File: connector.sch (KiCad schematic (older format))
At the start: 3 parts, among them J1 DB26_Male_HighDensity_Mountin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, J6 Conn_02x02_Odd_Even, SW3 SW_DIP_x03

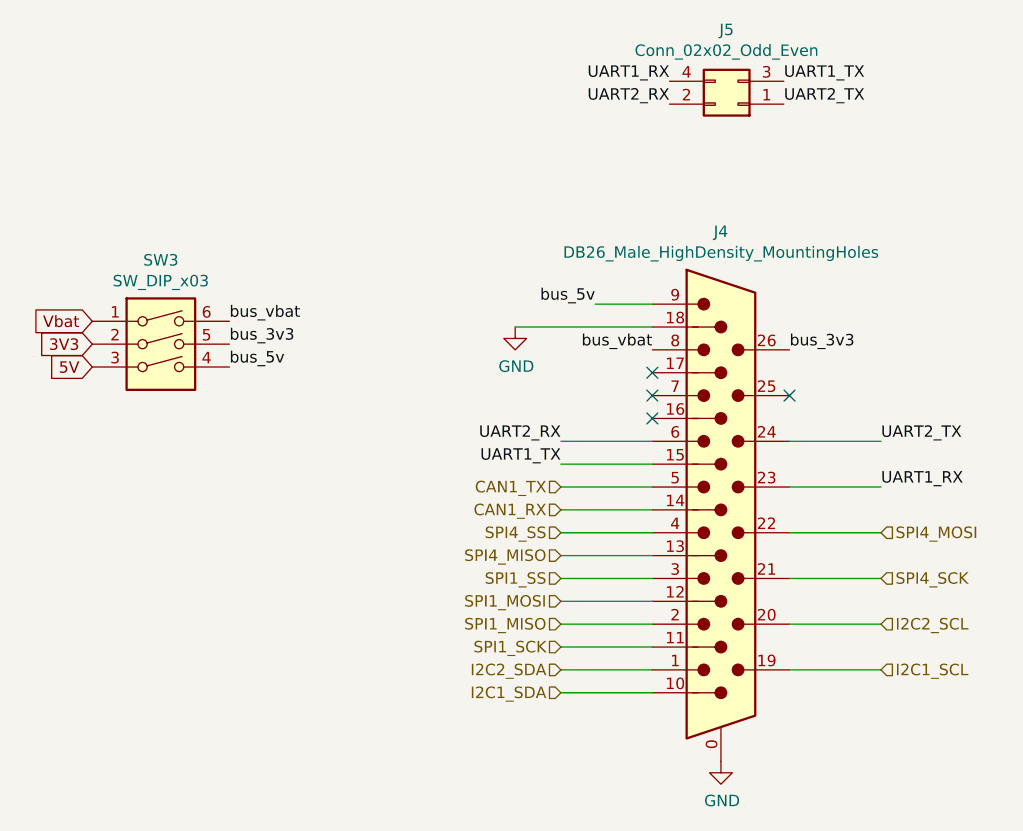
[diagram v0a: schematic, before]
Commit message: Change DB-26-HD footprint to match what we want
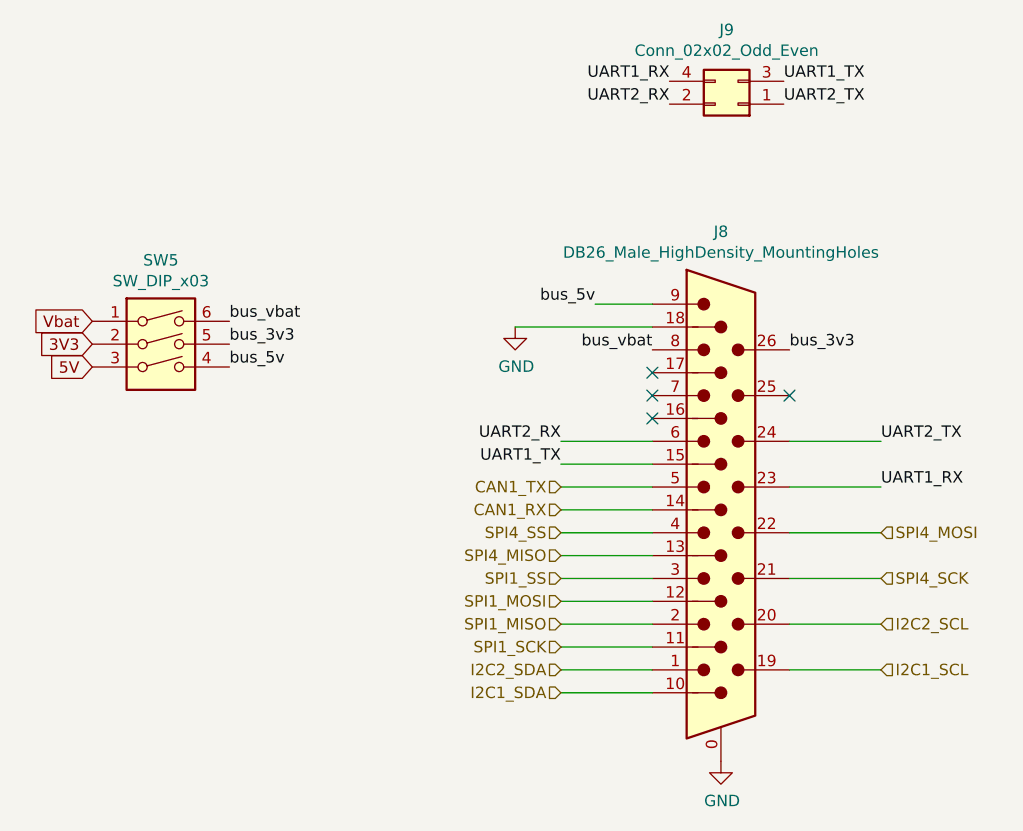
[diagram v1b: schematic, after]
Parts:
- J1: footprint Connector_Dsub:DSUB-26-HD_Male_Horizontal_P2.29x1.98mm_EdgePinOffset3.03mm_Housed_MountingHolesOffset4.94mm -> DB-HD-26:DSUB-26-HD_Male_Horizontal_P2.29x1.98mm_EdgePinOffset8.35mm_Housed_MountingHolesOffset10.89mm
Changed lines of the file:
@@
 $Descr A4 11693 8268
 encoding utf-8
-Sheet 3 9
+Sheet 5 9
 Title ""
 Date ""
@@
 AR Path="/5F237BED/5F14DCB5" Ref="J14"  Part="1"
 AR Path="/5F237C19/5F14DCB5" Ref="J16"  Part="1"
-F 0 "J4" H 5425 6217 50  0000 C CNN
+F 0 "J8" H 5425 6217 50  0000 C CNN
 F 1 "DB26_Male_HighDensity_MountingHoles" H 5425 6126 50  0000 C CNN
-F 2 "Connector_Dsub:DSUB-26-HD_Male_Horizontal_P2.29x1.98mm_EdgePinOffset3.03mm_Housed_MountingHolesOffset4.94mm" H 4475 5000 50  0001 C CNN
-F 3 " ~" H 4475 5000 50  0001 C CNN
+F 2 "DB-HD-26:DSUB-26-HD_Male_Horizontal_P2.29x1.98mm_EdgePinOffset8.35mm_Housed_MountingHolesOffset10.89mm" H 4475 5000 50  0001 C CNN
+F 3 "https://www.mouser.fr/ProductDetail/Kycon/K66X-A26S-N?qs=C%252BuF95oynlmx3ziDhlO2Bg%3D%3D" H 4475 5000 50  0001 C CNN
 	1    5425 4600
 	1    0    0    -1
@@
 AR Path="/5F237BED/5F139BC3" Ref="J15"  Part="1"
 AR Path="/5F237C19/5F139BC3" Ref="J17"  Part="1"
-F 0 "J5" H 5550 2100 50  0000 C CNN
+F 0 "J9" H 5550 2100 50  0000 C CNN
 F 1 "Conn_02x02_Odd_Even" H 5550 2191 50  0000 C CNN
 F 2 "Connector_PinHeader_2.54mm:PinHeader_2x02_P2.54mm_Vertical" H 5500 2425 50  0001 C CNN
@@
 AR Path="/5F237BED/5F4B7169" Ref="#PWR0120"  Part="1"
 AR Path="/5F237C19/5F4B7169" Ref="#PWR0123"  Part="1"
-F 0 "#PWR0105" H 4525 3150 50  0001 C CNN
+F 0 "#PWR0111" H 4525 3150 50  0001 C CNN
 F 1 "GND" H 4530 3227 50  0000 C CNN
 F 2 "" H 4525 3400 50  0001 C CNN
@@
 AR Path="/5F237BED/5F4B88F0" Ref="#PWR0121"  Part="1"
 AR Path="/5F237C19/5F4B88F0" Ref="#PWR0124"  Part="1"
-F 0 "#PWR0106" H 5425 5050 50  0001 C CNN
+F 0 "#PWR0112" H 5425 5050 50  0001 C CNN
 F 1 "GND" H 5430 5127 50  0000 C CNN
 F 2 "" H 5425 5300 50  0001 C CNN
@@
 AR Path="/5F237BED/5F14E492" Ref="SW8"  Part="1"
 AR Path="/5F237C19/5F14E492" Ref="SW9"  Part="1"
-F 0 "SW3" H 2975 4042 50  0000 C CNN
+F 0 "SW5" H 2975 4042 50  0000 C CNN
 F 1 "SW_DIP_x03" H 2975 3951 50  0000 C CNN
 F 2 "Button_Switch_THT:SW_DIP_SPSTx03_Slide_9.78x9.8mm_W7.62mm_P2.54mm" H 2975 3575 50  0001 C CNN
